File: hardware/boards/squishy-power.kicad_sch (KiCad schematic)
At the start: 92 parts, among them U1 W25N01GVZEIG, U10 FXL4TD245BQX, U11 FXL4TD245BQX, U12 FXL4TD245BQX, U13 FXL4TD245BQX, U14 FXL4TD245BQX, U15 FXL4TD245BQX, U16 FXL4TD245BQX, U17 THVD1452DGSR, U18 THVD1452DGSR, U19 THVD1452DGSR, U20 THVD1452DGSR, U21 THVD1452DGSR, U22 THVD1452DGSR, U23 THVD1452DGSR, U24 THVD1452DGSR, U25 THVD1452DGSR, U26 THVD1452DGSR, U27 THVD1452DGSR, U28 THVD1452DGSR, U29 THVD1452DGSR, U30 THVD1452DGSR, U31 THVD1452DGSR, U32 THVD1452DGSR, U33 THVD1452DGSR, U34 THVD1452DGSR, U4 TLV73312PQDRVRQ1, U5 LP5910-1.8DRVR, U7 TLV755533PDRVR, U8 FXL4TD245BQX, U9 FXL4TD245BQX

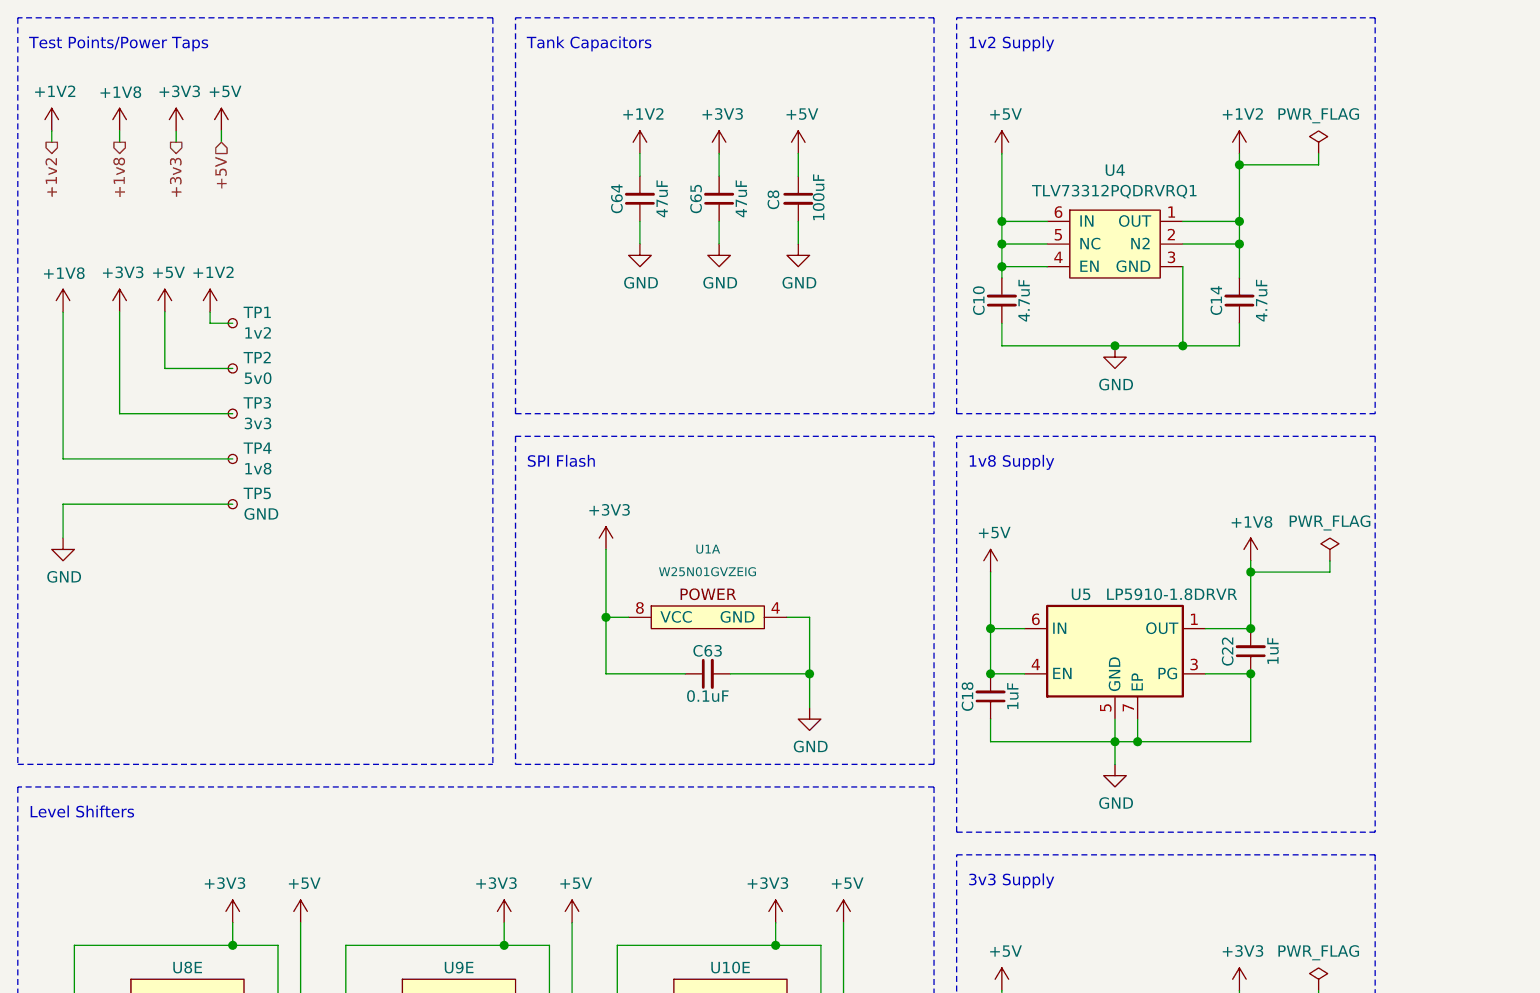
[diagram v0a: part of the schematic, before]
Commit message: hardware: Gutted the ULPI interface in favor of directly driving the USB diff pair due to gateware timing issues
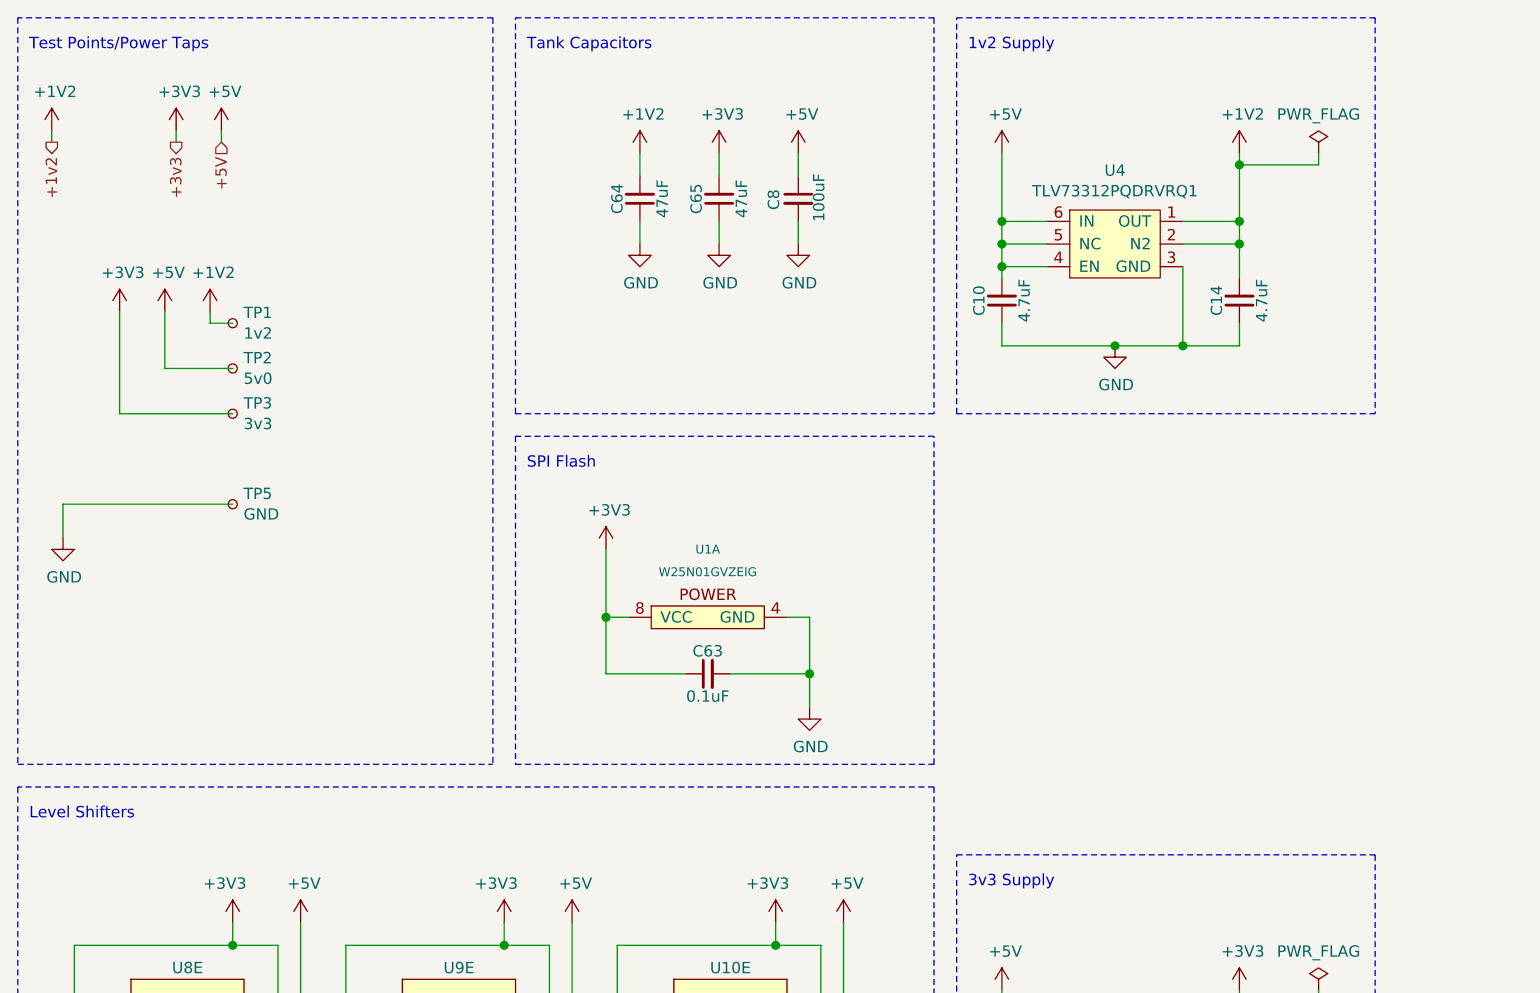
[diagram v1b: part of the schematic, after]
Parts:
- removed C18, C22: 1uF, Capacitor_SMD:C_0603_1608Metric, symbol Device:C_Small
- removed TP4: 1v8, TestPoint:TestPoint_Pad_D1.0mm, symbol Connector:TestPoint_Small
- removed U5: LP5910-1.8DRVR, Package_SON:WSON-6-1EP_2x2mm_P0.65mm_EP1x1.6mm_ThermalVias, symbol Regulator_Linear:LP5912-1.8DRV
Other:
- note removed: "1v8 Supply"
